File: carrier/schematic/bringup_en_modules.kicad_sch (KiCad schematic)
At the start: 44 parts, among them U201 SN74LVC1G08, U202 SN74LVC1G08, U203 SN74LVC1G08, U204 SN74LVC1G08, U205 SN74LVC1G08, U206 SN74LVC1G08, U207 SN74LVC1G08, U208 SN74LVC1G08, U209 SN74LVC1G08

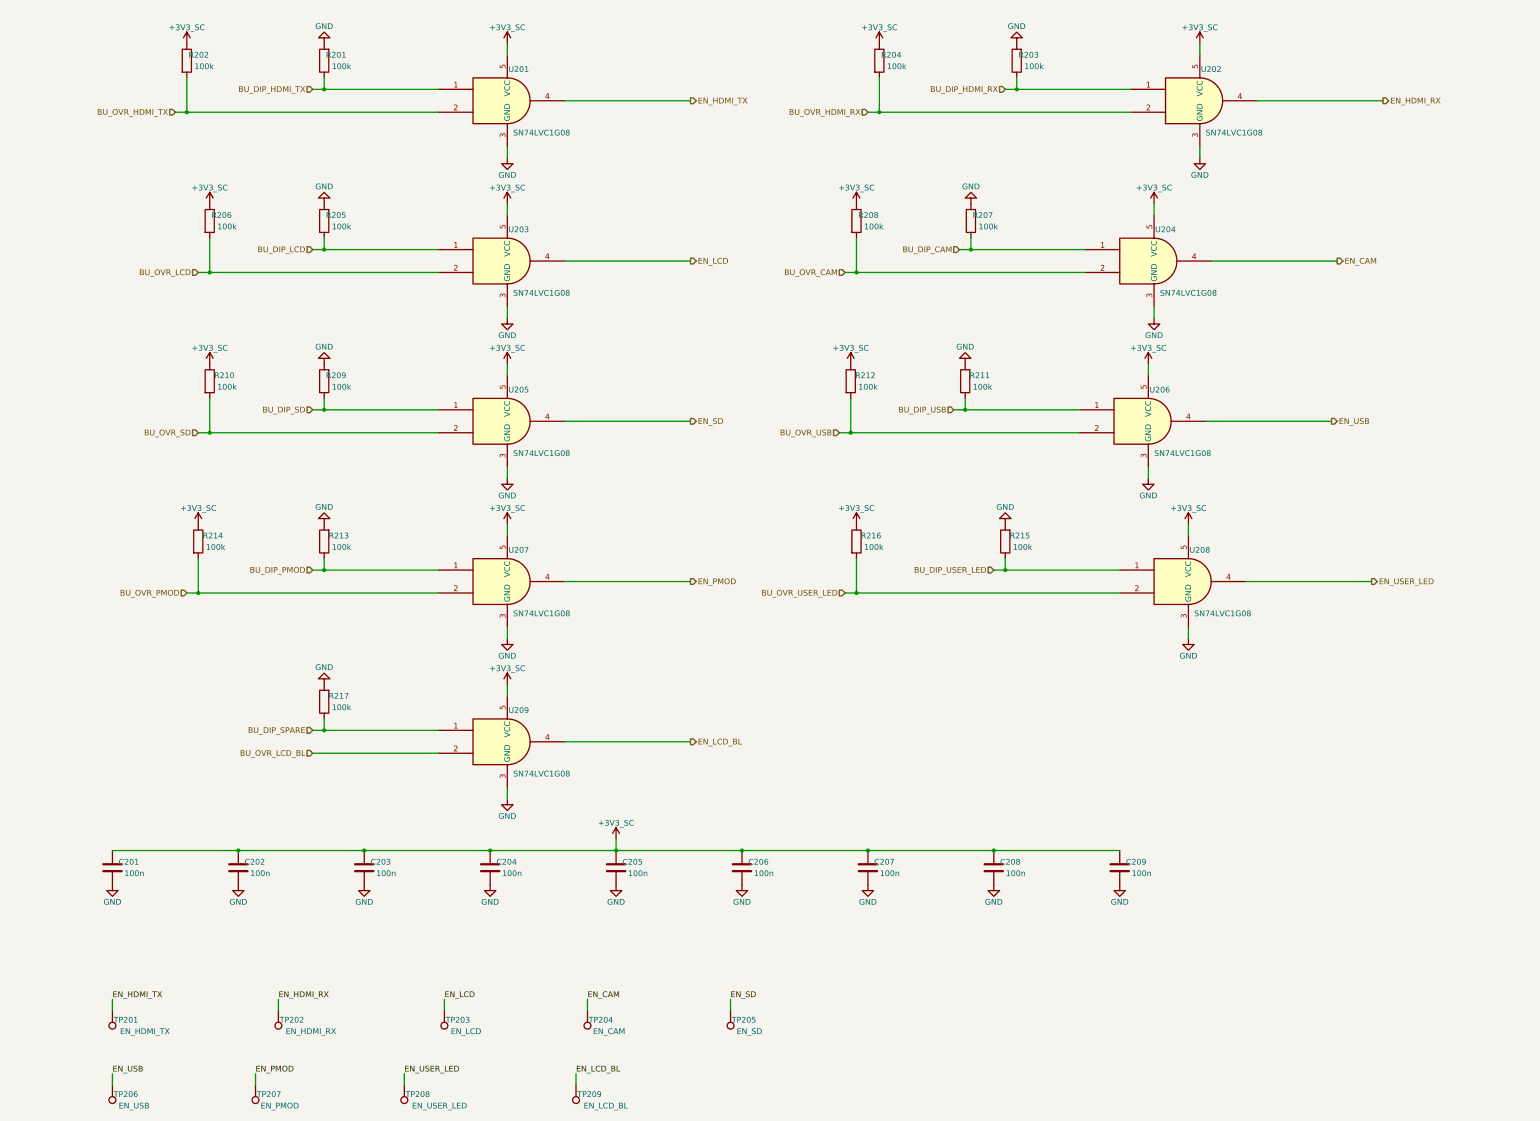
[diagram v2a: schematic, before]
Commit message: bringup: 5V MODULE GATES (PLAN round 5) — +5V_HDMI_TX/+5V_LCD SY6280 cells
Two new module gate cells resolve the power tree's last two UNSOURCED
findings, following the existing per-module pattern exactly:
- bringup_modules U9 +5V -> +5V_HDMI_TX (RSET 13k = 523 mA backstop; the
  load is TPD12S016-internally limited to 55 mA, DS 7.3.10) and U10
  +5V -> +5V_LCD (RSET 6.8k = 1.0 A for the 450 mA boost budget), 100n
  in/out, 1k status LEDs, TPs at the gated source.
- bringup_en_modules: 2 new SN74LVC1G08 AND cells (DIP master, SW veto).
- bringup_rails: SW1/SW2 positions were EXHAUSTED -> honest extension DIP
  SW6 (DSHP04TSGER, already-verified part; pos 1/2 wired, 3/4 author-NC
  spares) + TCA9535 P12/P13 vetos (P11 stays reserved for PMON_ALERT_N).
- bringup_facts.dip_switch_refs(): manual/firmware generators now discover
  every DSHP DIP instead of hard-coding SW1/SW2 — BRINGUP.md + the SC
  contract header regenerated with the new EN map automatically
  (ZC_TCA9535_BIT_EN_HDMI_TX_5V=10 / _EN_LCD_5V=11, SW6 stage-4 rows).
POWER TREE PASS: 14 regulators, findings 4->2, +5V buck at 91 % of 3 A.
All gates green (board exit 0); 3 drifted renders eyeballed full-res and
blessed; PWR_FLAG policy auto-stripped the now-driven rails' flags.

Co-Authored-By: Claude Fable 5 <noreply@anthropic.com>
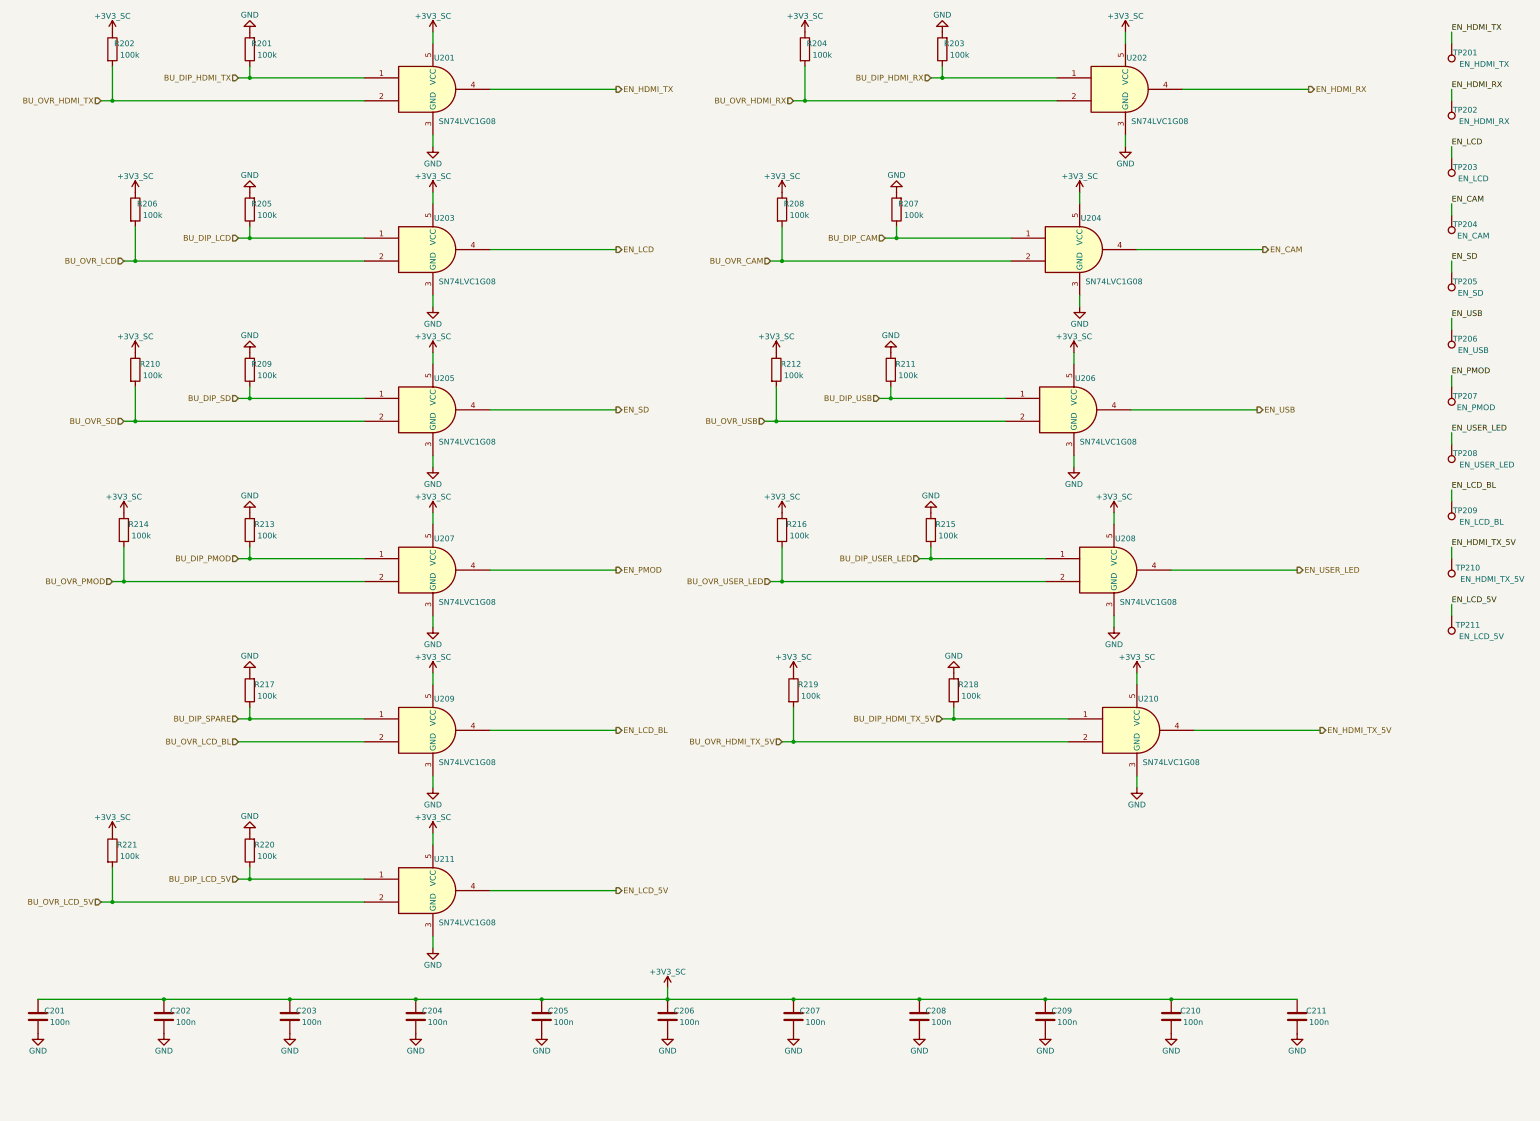
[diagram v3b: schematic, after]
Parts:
- added TP202: EN_HDMI_RX, TestPoint:TestPoint_Pad_D1.5mm, symbol Connector:TestPoint
- added TP203: EN_LCD, TestPoint:TestPoint_Pad_D1.5mm, symbol Connector:TestPoint
- added TP204: EN_CAM, TestPoint:TestPoint_Pad_D1.5mm, symbol Connector:TestPoint
- added TP205: EN_SD, TestPoint:TestPoint_Pad_D1.5mm, symbol Connector:TestPoint
- added TP206: EN_USB, TestPoint:TestPoint_Pad_D1.5mm, symbol Connector:TestPoint
- added TP207: EN_PMOD, TestPoint:TestPoint_Pad_D1.5mm, symbol Connector:TestPoint
- added TP208: EN_USER_LED, TestPoint:TestPoint_Pad_D1.5mm, symbol Connector:TestPoint
- added TP209: EN_LCD_BL, TestPoint:TestPoint_Pad_D1.5mm, symbol Connector:TestPoint
- added TP210: EN_HDMI_TX_5V, TestPoint:TestPoint_Pad_D1.5mm, symbol Connector:TestPoint
- added TP211: EN_LCD_5V, TestPoint:TestPoint_Pad_D1.5mm, symbol Connector:TestPoint
- C204: renamed from TP201; value EN_HDMI_TX -> 100n; footprint TestPoint:TestPoint_Pad_D1.5mm -> Capacitor_SMD:C_0603_1608Metric; symbol Connector:TestPoint -> Device:C; BOM exclude -> (none); LCSC (none) -> C1591
- C205: renamed from TP202; value EN_HDMI_RX -> 100n; footprint TestPoint:TestPoint_Pad_D1.5mm -> Capacitor_SMD:C_0603_1608Metric; symbol Connector:TestPoint -> Device:C; BOM exclude -> (none); LCSC (none) -> C1591
- C206: renamed from TP203; value EN_LCD -> 100n; footprint TestPoint:TestPoint_Pad_D1.5mm -> Capacitor_SMD:C_0603_1608Metric; symbol Connector:TestPoint -> Device:C; BOM exclude -> (none); LCSC (none) -> C1591
- C207: renamed from TP204; value EN_CAM -> 100n; footprint TestPoint:TestPoint_Pad_D1.5mm -> Capacitor_SMD:C_0603_1608Metric; symbol Connector:TestPoint -> Device:C; BOM exclude -> (none); LCSC (none) -> C1591
- C208: renamed from TP205; value EN_SD -> 100n; footprint TestPoint:TestPoint_Pad_D1.5mm -> Capacitor_SMD:C_0603_1608Metric; symbol Connector:TestPoint -> Device:C; BOM exclude -> (none); LCSC (none) -> C1591
- C209: renamed from TP206; value EN_USB -> 100n; footprint TestPoint:TestPoint_Pad_D1.5mm -> Capacitor_SMD:C_0603_1608Metric; symbol Connector:TestPoint -> Device:C; BOM exclude -> (none); LCSC (none) -> C1591
- C210: renamed from TP207; value EN_PMOD -> 100n; footprint TestPoint:TestPoint_Pad_D1.5mm -> Capacitor_SMD:C_0603_1608Metric; symbol Connector:TestPoint -> Device:C; BOM exclude -> (none); LCSC (none) -> C1591
- C211: renamed from TP208; value EN_USER_LED -> 100n; footprint TestPoint:TestPoint_Pad_D1.5mm -> Capacitor_SMD:C_0603_1608Metric; symbol Connector:TestPoint -> Device:C; BOM exclude -> (none); LCSC (none) -> C1591
- R218: renamed from C202; value 100n -> 100k; footprint Capacitor_SMD:C_0603_1608Metric -> Resistor_SMD:R_0603_1608Metric; symbol Device:C -> Device:R; LCSC C1591 -> C25803
- R219: renamed from C203; value 100n -> 100k; footprint Capacitor_SMD:C_0603_1608Metric -> Resistor_SMD:R_0603_1608Metric; symbol Device:C -> Device:R; LCSC C1591 -> C25803
- R220: renamed from C205; value 100n -> 100k; footprint Capacitor_SMD:C_0603_1608Metric -> Resistor_SMD:R_0603_1608Metric; symbol Device:C -> Device:R; LCSC C1591 -> C25803
- R221: renamed from C206; value 100n -> 100k; footprint Capacitor_SMD:C_0603_1608Metric -> Resistor_SMD:R_0603_1608Metric; symbol Device:C -> Device:R; LCSC C1591 -> C25803
- TP201: renamed from TP209; value EN_LCD_BL -> EN_HDMI_TX
- U210: renamed from C201; value 100n -> SN74LVC1G08; footprint Capacitor_SMD:C_0603_1608Metric -> Package_TO_SOT_SMD:SOT-23-5; symbol Device:C -> 74xGxx:74LVC1G08; LCSC C1591 -> C7666
- U211: renamed from C204; value 100n -> SN74LVC1G08; footprint Capacitor_SMD:C_0603_1608Metric -> Package_TO_SOT_SMD:SOT-23-5; symbol Device:C -> 74xGxx:74LVC1G08; LCSC C1591 -> C7666
- renumbered C207 to C201, C208 to C202, C209 to C203
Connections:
- net +3V3_SC: now also C204.1, C205.1, C206.1, C207.1, C208.1, C209.1, C210.1, C211.1, U210.5 (VCC), U211.5 (VCC); no longer R218.1, R220.1, U210.1, U211.1
- net EN_CAM: now also TP204.1; no longer C207.1
- net EN_HDMI_RX: now also TP202.1; no longer C205.1
- net EN_HDMI_TX: now also TP201.1; no longer C204.1
- net EN_LCD: now also TP203.1; no longer C206.1
- net EN_LCD_BL: now also TP209.1; no longer TP201.1
- net EN_PMOD: now also TP207.1; no longer C210.1
- net EN_SD: now also TP205.1; no longer C208.1
- net EN_USB: now also TP206.1; no longer C209.1
- net EN_USER_LED: now also TP208.1; no longer C211.1
- net GND: now also C204.2, C205.2, C206.2, C207.2, C208.2, C209.2, C210.2, C211.2, U210.3 (GND), U211.3 (GND); no longer R219.2, R221.2, U210.2, U211.2
- new net BU_DIP_HDMI_TX_5V: R218.1, U210.1
- new net BU_DIP_LCD_5V: R220.1, U211.1
- new net BU_OVR_HDMI_TX_5V: R219.2, U210.2
- new net BU_OVR_LCD_5V: R221.2, U211.2
- new net EN_HDMI_TX_5V: TP210.1, U210.4
- new net EN_LCD_5V: TP211.1, U211.4
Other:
- moved on the sheet: C201, C202, C203, R201, R202, R203, R204, R205, R206, R207, R208, R209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

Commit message: audit-fix(engine): harvest F1-F7,F9 — gate hardening + leak + guards
F1 selftest now exercises the VISUAL gate against geometry mutants (wire-cross
+ text-over-wire) — proven to bite (was never run on a mutant before).
F2 visual_gate catches different-net wire T-touch / butt-join shorts.
F3 netlist_gate no longer leaks tmp .net files (was 2671 stale).
F4 board uniquify guards the stride (widened 100->1000) against ref collision.
F5 hier-mode sheets now re-run through the per-sheet netlist gate.
F6 dead clause dropped; F7 stale zynq_eda docstring fixed; F9 eager inline-pin
validation. Source copied verbatim from the audit-fix worktree (6 files, proven
untouched on origin since its base); board regenerated fresh. All gates green,
selftest geo-mutants killed by the visual gate, goldens 23/23, m1_rc PASS.

Co-Authored-By: Claude Fable 5 <noreply@anthropic.com>
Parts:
- renumbered C201 to C2001, C202 to C2002, C203 to C2003, C204 to C2004, C205 to C2005, C206 to C2006, C207 to C2007, C208 to C2008, C209 to C2009, C210 to C2010, C211 to C2011, R201 to R2001, R202 to R2002, R203 to R2003, R204 to R2004, R205 to R2005, R206 to R2006, R207 to R2007, R208 to R2008, R209 to R2009, R210 to R2010, R211 to R2011, R212 to R2012, R213 to R2013, R214 to R2014, R215 to R2015, R216 to R2016, R217 to R2017, R218 to R2018, R219 to R2019, R220 to R2020, R221 to R2021, TP201 to TP2001, TP202 to TP2002, TP203 to TP2003, TP204 to TP2004, TP205 to TP2005, TP206 to TP2006, TP207 to TP2007, TP208 to TP2008, TP209 to TP2009, TP210 to TP2010, TP211 to TP2011, U201 to U2001, U202 to U2002, U203 to U2003, U204 to U2004, U205 to U2005, U206 to U2006, U207 to U2007, U208 to U2008, U209 to U2009, U210 to U2010, U211 to U2011

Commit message: genpolish: TITLE-1 — populate the schematic title block on every sheet
Every sheet rendered a blank Title/Rev/Date — the clearest 'not a real
schematic' tell. emit() now writes a (title_block ...) after the paper node:
title = the sheet circuit's title, company "Zynq SoM Carrier", and a
"<sheet> — generated by schgen (do not hand-edit)" comment. NO date node — a
wall-clock date would break byte-determinism; the content-derived fields keep
every rebuild identical. Verified on A4 (usb_pd) and the dense A3 (power): the
block fills the standard reserved corner with zero drawing overlap. All 26
sheets, goldens re-blessed, board PASS + deterministic, selftest 53/53, m1,
pytest 147.

Co-Authored-By: Claude Opus 4.8 <noreply@anthropic.com>
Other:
- company: (none) -> Zynq SoM Carrier
- title: (none) -> Bring-up EN cells: 11x SN74LVC1G08 module DIP-AND-override
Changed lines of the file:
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@@
 	(generator_version "1.0")
 	(paper "A3")
+	(title_block
+		(title "Bring-up EN cells: 11x SN74LVC1G08 module DIP-AND-override")
+		(company "Zynq SoM Carrier")
+		(comment 1 "bringup_en_modules — generated by schgen (do not hand-edit)")
+	)
 	(wire
 		(pts

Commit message: board: four board-management HW blocks on a manually-gated +3V3_AUX (BOARDHW)
The four services the carrier was missing — all behind ONE manual power enable
(C1) on two new sheets split so neither defeats the placer's rail-stub router:

  board_aux       — the gate + I2C isolator (infrastructure)
  board_services  — ID-EEPROM + RTC + watchdog + QWIIC (the peripherals)

WHAT LANDED
  * 24AA025E48 (C129895)  ID-EEPROM with a factory EUI-48 **MAC** for the
      LAN8720/RJ45 — strapped 0x51 (0x50 is the FMC EEPROM).
  * RV-3028-C7 (C3019759) I2C RTC, integrated DTCXO (no crystal), CR1220 coin
      cell (KH-CR1220-2) with auto-switchover, 0x52.
  * TPS3823-33 (C7719)    supervisor + windowed watchdog.
  * ZX-SH1.0-4PWT (C7430446)  QWIIC / STEMMA-QT expansion (gated 3V3 + the
      isolated AUX I2C).
  * SY6280 gate + DSHP04 DIP + PCA9306 isolator complete the infrastructure.

CONSTRAINTS (the user's three standing requirements)
  C1 manual enable "like the previous": +3V3_AUX is a SY6280 load switch whose
     EN is a default-OFF DSHP04 DIP (100k pulldown) — the same gated-module
     idiom, self-contained so it touches none of the dense rail/EN sheets.
  C2 "no watchdog reset during power-up": THREE independent guards — (1) the
     supervisor's VDD is the default-OFF +3V3_AUX, so it is UNPOWERED through
     power-up; (2) the TPS3823 disables its watchdog while WDI floats, and WDI
     is driven only by the PL (WATCHDOG_KICK, Hi-Z until the fabric is up); (3)
     RESET# is a firmware-mediated PL EVENT (J3.31), never a rail/POR line.
  C3 Zynq-agnostic: the only SoM-side signals (the 2 watchdog lines) ride PL
     bank-35 IO by their contract net names (IO_L16_N/P_35 -> J3.29/31); xdc.py
     emits the constraints live — nothing hard-codes the Zynq part.

LAW 0 (electrical integrity): the peripherals sit on the GATED rail but their
bus is the always-on STM32_I2C2 management bus. A PCA9306 bridges them with EN
tied to +3V3_AUX, so the switch OPENS whenever the rail is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
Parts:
- renumbered C2001 to C4001, C2002 to C4002, C2003 to C4003, C2004 to C4004, C2005 to C4005, C2006 to C4006, C2007 to C4007, C2008 to C4008, C2009 to C4009, C2010 to C4010, C2011 to C4011, R2001 to R4001, R2002 to R4002, R2003 to R4003, R2004 to R4004, R2005 to R4005, R2006 to R4006, R2007 to R4007, R2008 to R4008, R2009 to R4009, R2010 to R4010, R2011 to R4011, R2012 to R4012, R2013 to R4013, R2014 to R4014, R2015 to R4015, R2016 to R4016, R2017 to R4017, R2018 to R4018, R2019 to R4019, R2020 to R4020, R2021 to R4021, TP2001 to TP4001, TP2002 to TP4002, TP2003 to TP4003, TP2004 to TP4004, TP2005 to TP4005, TP2006 to TP4006, TP2007 to TP4007, TP2008 to TP4008, TP2009 to TP4009, TP2010 to TP4010, TP2011 to TP4011, U2001 to U4001, U2002 to U4002, U2003 to U4003, U2004 to U4004, U2005 to U4005, U2006 to U4006, U2007 to U4007, U2008 to U4008, U2009 to U4009, U2010 to U4010, U2011 to U4011

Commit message: audit fixes: QWIIC ESD on its own sheet + firmware I2C-map completeness
Acting on a multi-agent adversarial re-audit of the 28-sheet board. Each
finding was independently re-verified before action — two confident "HIGH"
findings were FALSE POSITIVES whose proposed fixes would have INTRODUCED bugs,
and are documented-rejected, not applied:

  * "DSHP04 switches in parallel" — wrong. The footprint pads prove the pairing
    by physical opposition (switch n = pads n & 9-n): switch 1 = pads 1&8 is the
    only one on EN_AUX; the other even pins (2/4/6) are NC, identical to the
    proven bringup_rails SW6 idiom. The proposed "fix" (pins 1+2) wires two
    DIFFERENT switches and would leave EN_AUX permanently pulled down — the rail
    could never enable.
  * "PCA9306 EN floats when AUX is off" — wrong. A 100k to a 0 V rail pulls EN
    to 0 V (disabled), which is exactly TI's recommended "isolate when the gated
    side is unpowered" connection. No float.

REAL findings actioned:

1. QWIIC connector lacked ESD (every other external connector has it). Moved the
   QWIIC out of board_services onto its own sheet board_qwiic (the carrier's
   connectors-get-their-own-sheet idiom — rj45_connector, usb_uart_connector)
   and added a USBLC6-2SC6 low-cap ESD array at the connector (1<->6 / 3<->4
   passthrough, clamp ref +3V3_AUX). The dedicated sheet also keeps both sheets
   sparse enough for the rail-stub router. board_services drops to 9 parts.

2. schgen/firmware.py loaded only 7 sheets, so the SC-firmware contract + its
   I2C address-collision check were BLIND to the new devices. Added board_aux/
   board_services to SOURCES and three address rows: FMC-EEPROM 0x50, ID-EEPROM
   0x51 (DERIVED from the 24AA025E48 A1/A0 straps, so a mis-strap to 0x50 now
   trips the collision check against the FMC EEPROM), RTC 0x52. The firmware can
   now address the EUI-48 MAC EEPROM and the RTC. 114 -> 117 #defines.

3. board_services docstring clarified (EEPROM/RTC are on the PCA9306-i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
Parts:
- renumbered C4001 to C5001, C4002 to C5002, C4003 to C5003, C4004 to C5004, C4005 to C5005, C4006 to C5006, C4007 to C5007, C4008 to C5008, C4009 to C5009, C4010 to C5010, C4011 to C5011, R4001 to R5001, R4002 to R5002, R4003 to R5003, R4004 to R5004, R4005 to R5005, R4006 to R5006, R4007 to R5007, R4008 to R5008, R4009 to R5009, R4010 to R5010, R4011 to R5011, R4012 to R5012, R4013 to R5013, R4014 to R5014, R4015 to R5015, R4016 to R5016, R4017 to R5017, R4018 to R5018, R4019 to R5019, R4020 to R5020, R4021 to R5021, TP4001 to TP5001, TP4002 to TP5002, TP4003 to TP5003, TP4004 to TP5004, TP4005 to TP5005, TP4006 to TP5006, TP4007 to TP5007, TP4008 to TP5008, TP4009 to TP5009, TP4010 to TP5010, TP4011 to TP5011, U4001 to U5001, U4002 to U5002, U4003 to U5003, U4004 to U5004, U4005 to U5005, U4006 to U5006, U4007 to U5007, U4008 to U5008, U4009 to U5009, U4010 to U5010, U4011 to U5011

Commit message: bom: sourcing risk+cost report + C1591->C14663 (Extended->Basic 100n)
Stream F — live JLCPCB/LCSC sourcing pass over all 95 distinct BOM parts.

Report: carrier/manufacturing/SOURCING.md — per-part stock / Basic-vs-Extended
/ unit price / risk + flagged second sources, and a rollup (94 parts post-swap,
64 Extended of which 2 Preferred -> 62 feeder fees = ~$186, 15 parts <5k stock,
6 procurement-critical <300). Data from the JLCPCB parts API (live).

Applied swap (only clean Basic drop-in on the board): 100 nF 0603 decoupling
C1591 (Samsung CL10B104KB8NNNC, Extended, 2.08M) -> C14663 (YAGEO
CC0603KRX7R9BB104, Basic, 17.8M). IDENTICAL 100nF/50V/X7R/+-10%/0603, same
footprint+symbol -> netlist & render byte-identical; ratings.py already carries
C14663 with matching ratings. Merges 71 Extended + 12 existing-Basic positions
onto one 83-piece Basic line: removes one Extended feeder fee, cheaper unit,
8.5x more stock.

Everything else is REPORT-ONLY: every other Extended part is
Extended-by-necessity (no JLC-Basic equivalent — precise E96 values, specialty
ICs/connectors) or has only a footprint-mismatched / MPN-ambiguous alternate.
Also flagged (not fixed): C25750 ("40.2k" power:R1) currently resolves on LCSC
to a 120k 0402 part — a data-integrity bug; recommend C12447 after intent check.

Gates: part-rules PASS (132 checks, 0 findings); board PASS (33 sheets, golden
renders 33/33 match, DRC 0); selftest 59/59; m1_rc PASS; pytest 219 passed.
BOM regen deterministic (md5 stable).

Co-Authored-By: Claude Opus 4.8 <noreply@anthropic.com>
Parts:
- C5001, C5002, C5003, C5004, C5005, C5006, C5007, C5008, C5009, C5010, C5011: LCSC C1591 -> C14663
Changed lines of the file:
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@@
 		(property
 			"LCSC"
-			"C1591"
+			"C14663"
 			(at 48.26 248.92 0)
 			(effects
@@
 		(property
 			"LCSC"
-			"C1591"
+			"C14663"
 			(at 76.2 248.92 0)
 			(effects
@@
 		(property
 			"LCSC"
-			"C1591"
+			"C14663"
 			(at 104.14 248.92 0)
 			(effects
@@
 		(property
 			"LCSC"
-			"C1591"
+			"C14663"
 			(at 132.08 248.92 0)
 			(effects
@@
 		(property
 			"LCSC"
-			"C1591"
+			"C14663"
 			(at 160.02 248.92 0)
 			(effects
@@
 		(property
 			"LCSC"
-			"C1591"
+			"C14663"
 			(at 187.96 248.92 0)
 			(effects
@@
 		(property
 			"LCSC"
-			"C1591"
+			"C14663"
 			(at 215.9 248.92 0)
 			(effects
@@
 		(property
 			"LCSC"
-			"C1591"
+			"C14663"
 			(at 243.84 248.92 0)
 			(effects
@@
 		(property
 			"LCSC"
-			"C1591"
+			"C14663"
 			(at 271.78 248.92 0)
 			(effects
@@
 		(property
 			"LCSC"
-			"C1591"
+			"C14663"
 			(at 299.72 248.92 0)
 			(effects
@@
 		(property
 			"LCSC"
-			"C1591"
+			"C14663"
 			(at 327.66 248.92 0)
 			(effects
